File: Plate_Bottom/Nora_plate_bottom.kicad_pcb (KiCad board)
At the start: 2 copper layers, 285 x 94.6 mm, 8 parts

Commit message: スペーサー配置箇所の銅箔除去。バージョン更新 #105 #120
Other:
- board text added: "Bottom Plate v.1.2.1 @jpskenn"
- board text removed: "Bottom Plate v.1.2 @jpskenn"
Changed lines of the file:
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@@
   (gr_line (start 13 106.9) (end 305 106.9) (layer "Eco1.User") (width 0.15))
   (gr_circle (center 40.62 44.97) (end 41.69 45.47) (layer "Eco1.User") (width 0.15) (fill none))
-  (gr_text "Bottom Plate v.1.2\n@jpskenn" (at 91 66) (layer "F.SilkS")
+  (gr_circle (center 40.62 44.97) (end 42.65 46.1) (layer "Eco1.User") (width 0.15) (fill none))
+  (gr_text "Bottom Plate v.1.2.1\n@jpskenn" (at 91 66) (layer "F.SilkS")
     (effects (font (size 1.8 1.8) (thickness 0.3)) (justify left))
   )
@@
   )
   (zone (net 0) (net_name "") (layer "F.Cu") (hatch edge 0.508)
+    (connect_pads (clearance 0))
+    (min_thickness 0.254)
+    (keepout (tracks not_allowed) (vias allowed) (pads allowed ) (copperpour not_allowed) (footprints allowed))
+    (fill (thermal_gap 0.508) (thermal_bridge_width 0.508))
+    (polygon
+      (pts
+        (xy 241.7 106.05)
+        (xy 241.710866 108.05)
+        (xy 240.110004 109.441086)
+        (xy 238.210004 109.441086)
+        (xy 236.650022 108.05)
+        (xy 236.65 106)
+        (xy 238.1 104.4)
+        (xy 240.3 104.4)
+      )
+    )
+  )
+  (zone (net 0) (net_name "") (layer "F.Cu") (hatch edge 0.508)
+    (connect_pads (clearance 0))
+    (min_thickness 0.254)
+    (keepout (tracks not_allowed) (vias allowed) (pads allowed ) (copperpour not_allowed) (footprints allowed))
+    (fill (thermal_gap 0.508) (thermal_bridge_width 0.508))
+    (polygon
+      (pts
+        (xy 301.407595 71.05)
+        (xy 301.4 76.1)
+        (xy 299.708592 76.106609)
+        (xy 295.768596 76.106609)
+        (xy 294.058614 74.715526)
+        (xy 294.058592 72.665526)
+        (xy 295.658592 71.065523)
+        (xy 299.708592 71.065523)
+      )
+    )
+  )
+  (zone (net 0) (net_name "") (layer "F.Cu") (hatch edge 0.508)
+    (connect_pads (clearance 0))
+    (min_thickness 0.254)
+    (keepout (tracks not_allowed) (vias allowed) (pads allowed ) (copperpour not_allowed) (footprints allowed))
+    (fill (thermal_gap 0.508) (thermal_bridge_width 0.508))
+    (polygon
+      (pts
+        (xy 203.35 106.05)
+        (xy 203.360866 108.05)
+        (xy 201.760004 109.441086)
+        (xy 199.860004 109.441086)
+        (xy 198.300022 108.05)
+        (xy 198.3 106)
+        (xy 199.75 104.4)
+        (xy 201.95 104.4)
+      )
+    )
+  )
+  (zone (net 0) (net_name "") (layer "F.Cu") (hatch edge 0.508)
+    (connect_pads (clearance 0))
+    (min_thickness 0.254)
+    (keepout (tracks not_allowed) (vias allowed) (pads allowed ) (copperpour not_allowed) (footprints allowed))
+    (fill (thermal_gap 0.508) (thermal_bridge_width 0.508))
+    (polygon
+      (pts
+        (xy 43.159437 44.1)
+        (xy 43.170303 46.1)
+        (xy 41.569441 47.491086)
+        (xy 39.669441 47.491086)
+        (xy 38.109459 46.1)
+        (xy 38.109437 44.05)
+        (xy 39.559437 42.45)
+        (xy 41.759437 42.45)
+      )
+    )
+  )
+  (zone (net 0) (net_name "") (layer "F.Cu") (hatch edge 0.508)
+    (connect_pads (clearance 0))
+    (min_thickness 0.254)
+    (keepout (tracks not_allowed) (vias allowed) (pads allowed ) (copperpour not_allowed) (footprints allowed))
+    (fill (thermal_gap 0.508) (thermal_bridge_width 0.508))
+    (polygon
+      (pts
+        (xy 279.160734 44.036815)
+        (xy 279.141093 46.036815)
+        (xy 277.461731 47.437137)
+        (xy 273.521735 47.437137)
+        (xy 271.811753 46.046054)
+        (xy 271.811731 43.996054)
+        (xy 273.411731 42.396051)
+        (xy 277.461731 42.396051)
+      )
+    )
+  )
+  (zone (net 0) (net_name "") (layer "F.Cu") (hatch edge 0.508)
+    (connect_pads (clearance 0))
+    (min_thickness 0.254)
+    (keepout (tracks not_allowed) (vias allowed) (pads allowed ) (copperpour not_allowed) (footprints allowed))
+    (fill (thermal_gap 0.508) (thermal_bridge_width 0.508))
+    (polygon
+      (pts
+        (xy 21.707595 72.656287)
+        (xy 21.687954 74.656287)
+        (xy 20.008592 76.056609)
+        (xy 16.068596 76.056609)
+        (xy 14.4 76.05)
+        (xy 14.358592 71)
+        (xy 15.958592 71.015523)
+        (xy 20.008592 71.015523)
+      )
+    )
+  )
+  (zone (net 0) (net_name "") (layer "F.Cu") (hatch edge 0.508)
+    (connect_pads (clearance 0))
+    (min_thickness 0.254)
+    (keepout (tracks not_allowed) (vias allowed) (pads allowed ) (copperpour not_allowed) (footprints allowed))
+    (fill (thermal_gap 0.508) (thermal_bridge_width 0.508))
+    (polygon
+      (pts
+        (xy 209.607595 101.406287)
+        (xy 209.587954 103.406287)
+        (xy 207.908592 104.806609)
+        (xy 203.968596 104.806609)
+        (xy 202.258614 103.415526)
+        (xy 202.258592 101.365526)
+        (xy 203.858592 99.765523)
+        (xy 207.908592 99.765523)
+      )
+    )
+  )
+  (zone (net 0) (net_name "") (layer "F.Cu") (hatch edge 0.508)
+    (connect_pads (clearance 0))
+    (min_thickness 0.254)
+    (keepout (tracks not_allowed) (vias allowed) (pads allowed ) (copperpour not_allowed) (footprints allowed))
+    (fill (thermal_gap 0.508) (thermal_bridge_width 0.508))
+    (polygon
+      (pts
+        (xy 112.85 20.45)
+        (xy 112.860866 22.45)
+        (xy 111.260004 23.841086)
+        (xy 109.360004 23.841086)
+        (xy 107.800022 22.45)
+        (xy 107.8 20.4)
+        (xy 109.25 18.8)
+        (xy 111.45 18.8)
+      )
+    )
+  )
+  (zone (net 0) (net_name "") (layer "F.Cu") (hatch edge 0.508)
     (connect_pads (clearance 0.508))
-    (min_thickness 0.254)
+    (min_thickness 0.254) (filled_areas_thickness no)
     (fill yes (thermal_gap 0.508) (thermal_bridge_width 0.508))
     (polygon
@@
     )
   )
+  (zone (net 0) (net_name "") (layer "F.Cu") (hatch edge 0.508)
+    (connect_pads (clearance 0))
+    (min_thickness 0.254)
+    (keepout (tracks not_allowed) (vias allowed) (pads allowed ) (copperpour not_allowed) (footprints allowed))
+    (fill (thermal_gap 0.508) (thermal_bridge_width 0.508))
+    (polygon
+      (pts
+        (xy 208.1 20.45)
+        (xy 208.110866 22.45)
+        (xy 206.510004 23.841086)
+        (xy 204.610004 23.841086)
+        (xy 203.050022 22.45)
+        (xy 203.05 20.4)
+        (xy 204.5 18.8)
+        (xy 206.7 18.8)
+      )
+    )
+  )
+  (zone (net 0) (net_name "") (layer "F.Cu") (hatch edge 0.508)
+    (connect_pads (clearance 0))
+    (min_thickness 0.254)
+    (keepout (tracks not_allowed) (vias allowed) (pads allowed ) (copperpour not_allowed) (footprints allowed))
+    (fill (thermal_gap 0.508) (thermal_bridge_width 0.508))
+    (polygon
+      (pts
+        (xy 147.299003 63.190764)
+        (xy 147.279362 65.190764)
+        (xy 145.6 66.591086)
+        (xy 141.660004 66.591086)
+        (xy 139.950022 65.200003)
+        (xy 139.95 63.150003)
+        (xy 141.55 61.55)
+        (xy 145.6 61.55)
+      )
+    )
+  )
+  (zone (net 0) (net_name "") (layer "F.Cu") (hatch edge 0.508)
+    (connect_pads (clearance 0))
+    (min_thickness 0.254)
+    (keepout (tracks not_allowed) (vias allowed) (pads allowed ) (copperpour not_allowed) (footprints allowed))
+    (fill (thermal_gap 0.508) (thermal_bridge_width 0.508))
+    (polygon
+      (pts
+        (xy 101.8 106.05)
+        (xy 101.810866 108.05)
+        (xy 100.210004 109.441086)
+        (xy 98.310004 109.441086)
+        (xy 96.750022 108.05)
+        (xy 96.75 106)
+        (xy 98.2 104.4)
+        (xy 100.4 104.4)
+      )
+    )
+  )
   (zone (net 0) (net_name "") (layer "B.Cu") (hatch edge 0.508)
     (connect_pads (clearance 0.508))
-    (min_thickness 0.254)
+    (min_thickness 0.254) (filled_areas_thickness no)
     (fill yes (thermal_gap 0.508) (thermal_bridge_width 0.508))
     (polygon

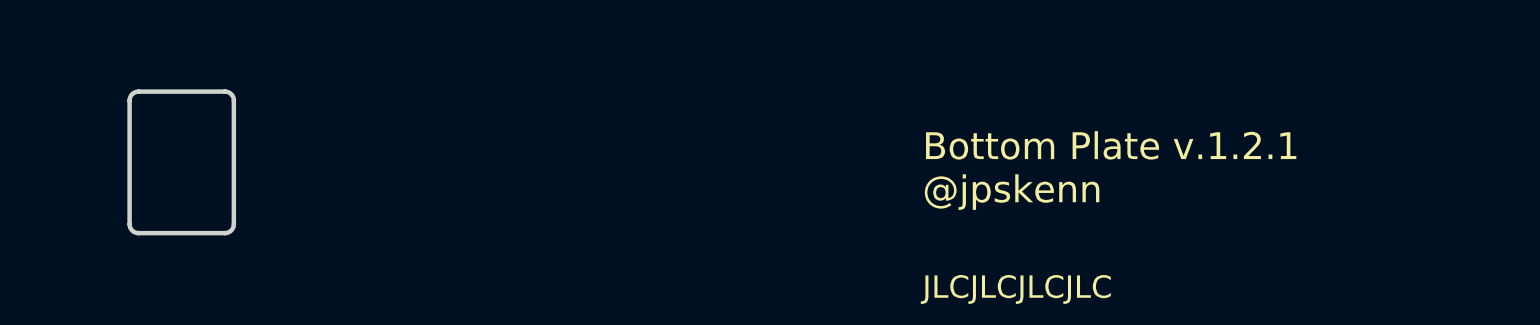
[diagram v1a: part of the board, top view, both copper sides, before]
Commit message: ボトムのリセット穴を拡大して、Noraのリセットスイッチを押せるようにした #132
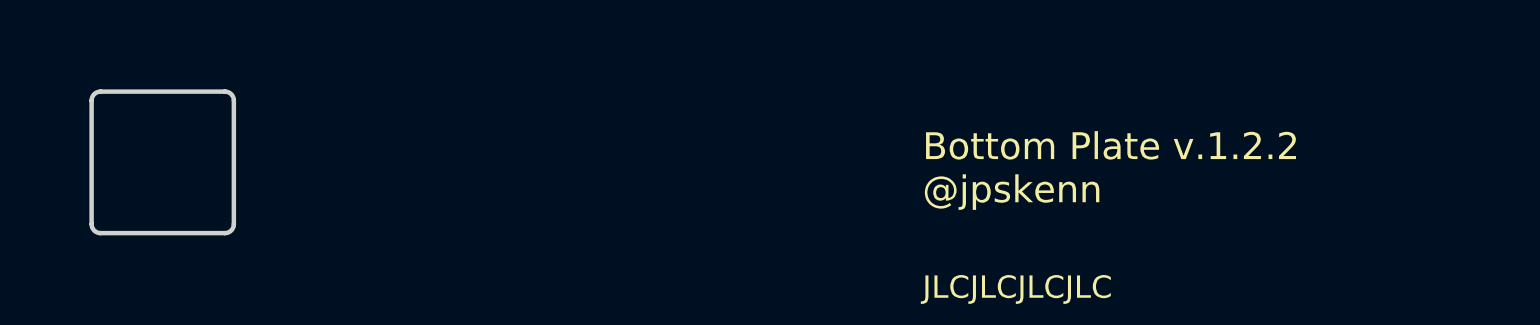
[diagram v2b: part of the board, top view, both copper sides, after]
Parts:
- REF**: footprint locallib:60_Outline_Nora_with_PICO_ -> locallib:60_Outline_Nora_with_PICO_large_reset_hole
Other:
- outline, holes or cut-outs redrawn
- board text added: "Bottom Plate v.1.2.2 @jpskenn"
- board text removed: "Bottom Plate v.1.2.1 @jpskenn"

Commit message: プレート類のガーバーファイル準備
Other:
- board text added: "Bottom Plate v.1.2.2 for #Jones_kbd & #Nora_kbd @jpskenn"
- board text removed: "Bottom Plate v.1.2.2 @jpskenn"
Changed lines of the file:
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@@
   (gr_circle (center 40.62 44.97) (end 41.69 45.47) (layer "Eco1.User") (width 0.15) (fill none))
   (gr_circle (center 40.62 44.97) (end 42.65 46.1) (layer "Eco1.User") (width 0.15) (fill none))
-  (gr_text "Bottom Plate v.1.2.2\n@jpskenn" (at 91 66) (layer "F.SilkS")
-    (effects (font (size 1.8 1.8) (thickness 0.3)) (justify left))
+  (gr_text "Bottom Plate v.1.2.2\nfor #Jones_kbd & #Nora_kbd\n@jpskenn" (at 91 66) (layer "F.SilkS")
+    (effects (font (size 1.8 1.8) (thickness 0.24)) (justify left))
   )
   (gr_text "JLCJLCJLCJLC" (at 91 74) (layer "F.SilkS")
